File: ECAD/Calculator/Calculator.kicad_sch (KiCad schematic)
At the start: 30 parts, among them SW1 Switch_Tactile_ESwitch, SW10 Switch_Tactile_ESwitch, SW11 Switch_Tactile_ESwitch, SW12 Switch_Tactile_ESwitch, SW13 Switch_Tactile_ESwitch, SW14 Switch_Tactile_ESwitch, SW15 Switch_Tactile_ESwitch, SW16 Switch_Tactile_ESwitch, SW17 Switch_Tactile_ESwitch, SW18 Switch_Tactile_ESwitch, SW19 Switch_Tactile_ESwitch, SW2 Switch_Tactile_ESwitch, SW20 Switch_Tactile_ESwitch, SW3 Switch_Tactile_ESwitch, SW4 Switch_Tactile_ESwitch, SW5 Switch_Tactile_ESwitch, SW6 Switch_Tactile_ESwitch, SW7 Switch_Tactile_ESwitch, SW8 Switch_Tactile_ESwitch, SW9 Switch_Tactile_ESwitch

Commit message: Refactor Calculator schematic and library components
- Added multiple no-connect points in the Calculator schematic for better layout management.
- Updated the footprint properties for buttons to use "Button_Switch_Keyboard:SW_Cherry_MX_1.00u_PCB" instead of the previous "PCM_fab:Button_ESwitch_TL3315NF100Q_4.5x4.5mm".
- Introduced a new footprint for solder pads in the Calculator library.
- Created a new footprint library table for the Calculator project.
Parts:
- SW1, SW10, SW11, SW12, SW13, SW14, SW15, SW16, SW17, SW18, SW19, SW2, SW20, SW3, SW4, SW5, SW6, SW7, SW8, SW9: footprint PCM_fab:Button_ESwitch_TL3315NF100Q_4.5x4.5mm -> Button_Switch_Keyboard:SW_Cherry_MX_1.00u_PCB
- TP1, TP2, TP3, TP4, TP5, TP6, TP7, TP8, TP9: footprint (none) -> Calculator_lib:Solder_pad
- U1: footprint ESP32_30pin -> ESP32_Footprints:ESP32_30pin
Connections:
- no-connect marks 0 -> 12
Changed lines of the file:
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@@
 		(color 0 0 0 0)
 	)
+	(no_connect
+		(at 80.01 31.75)
+	)
+	(no_connect
+		(at 53.34 44.45)
+	)
+	(no_connect
+		(at 80.01 62.23)
+	)
+	(no_connect
+		(at 80.01 29.21)
+	)
+	(no_connect
+		(at 53.34 62.23)
+	)
+	(no_connect
+		(at 53.34 57.15)
+	)
+	(no_connect
+		(at 53.34 54.61)
+	)
+	(no_connect
+		(at 80.01 64.77)
+	)
+	(no_connect
+		(at 80.01 57.15)
+	)
+	(no_connect
+		(at 80.01 59.69)
+	)
+	(no_connect
+		(at 53.34 59.69)
+	)
+	(no_connect
+		(at 53.34 34.29)
+	)
 	(wire
 		(pts
@@
 			)
 		)
-		(property "Footprint" "PCM_fab:Button_ESwitch_TL3315NF100Q_4.5x4.5mm"
+		(property "Footprint" "Button_Switch_Keyboard:SW_Cherry_MX_1.00u_PCB"
 			(at 175.26 55.88 0)
 			(hide yes)
@@
 			)
 		)
-		(property "Footprint" "PCM_fab:Button_ESwitch_TL3315NF100Q_4.5x4.5mm"
+		(property "Footprint" "Button_Switch_Keyboard:SW_Cherry_MX_1.00u_PCB"
 			(at 129.54 78.74 0)
 			(hide yes)
@@
 			)
 		)
-		(property "Footprint" "PCM_fab:Button_ESwitch_TL3315NF100Q_4.5x4.5mm"
+		(property "Footprint" "Button_Switch_Keyboard:SW_Cherry_MX_1.00u_PCB"
 			(at 129.54 44.45 0)
 			(hide yes)
@@
 			)
 		)
-		(property "Footprint" ""
+		(property "Footprint" "Calculator_lib:Solder_pad"
 			(at 25.4 39.37 0)
 			(hide yes)
@@
 			)
 		)
-		(property "Footprint" ""
+		(property "Footprint" "Calculator_lib:Solder_pad"
 			(at 25.4 16.51 0)
 			(hide yes)
@@
 			)
 		)
-		(property "Footprint" ""
+		(property "Footprint" "Calculator_lib:Solder_pad"
 			(at 25.4 31.75 0)
 			(hide yes)
@@
 			)
 		)
-		(property "Footprint" ""
+		(property "Footprint" "Calculator_lib:Solder_pad"
 			(at 25.4 43.18 0)
 			(hide yes)
@@
 			)
 		)
-		(property "Footprint" "PCM_fab:Button_ESwitch_TL3315NF100Q_4.5x4.5mm"
+		(property "Footprint" "Button_Switch_Keyboard:SW_Cherry_MX_1.00u_PCB"
 			(at 129.54 67.31 0)
 			(hide yes)
@@
 			)
 		)
-		(property "Footprint" ""
+		(property "Footprint" "Calculator_lib:Solder_pad"
 			(at 25.4 12.7 0)
 			(hide yes)
@@
 			)
 		)
-		(property "Footprint" "PCM_fab:Button_ESwitch_TL3315NF100Q_4.5x4.5mm"
+		(property "Footprint" "Button_Switch_Keyboard:SW_Cherry_MX_1.00u_PCB"
 			(at 106.68 33.02 0)
 			(hide yes)
@@
 			)
 		)
-		(property "Footprint" "PCM_fab:Button_ESwitch_TL3315NF100Q_4.5x4.5mm"
+		(property "Footprint" "Button_Switch_Keyboard:SW_Cherry_MX_1.00u_PCB"
 			(at 106.68 55.88 0)
 			(hide yes)
@@
 			)
 		)
-		(property "Footprint" "PCM_fab:Button_ESwitch_TL3315NF100Q_4.5x4.5mm"
+		(property "Footprint" "Button_Switch_Keyboard:SW_Cherry_MX_1.00u_PCB"
 			(at 152.4 55.88 0)
 			(hide yes)
@@
 			)
 		)
-		(property "Footprint" "PCM_fab:Button_ESwitch_TL3315NF100Q_4.5x4.5mm"
+		(property "Footprint" "Button_Switch_Keyboard:SW_Cherry_MX_1.00u_PCB"
 			(at 129.54 55.88 0)
 			(hide yes)
@@
 			)
 		)
-		(property "Footprint" "PCM_fab:Button_ESwitch_TL3315NF100Q_4.5x4.5mm"
+		(property "Footprint" "Button_Switch_Keyboard:SW_Cherry_MX_1.00u_PCB"
 			(at 175.26 44.45 0)
 			(hide yes)
@@
 			)
 		)
-		(property "Footprint" "PCM_fab:Button_ESwitch_TL3315NF100Q_4.5x4.5mm"
+		(property "Footprint" "Button_Switch_Keyboard:SW_Cherry_MX_1.00u_PCB"
 			(at 152.4 44.45 0)
 			(hide yes)
@@
 			)
 		)
-		(property "Footprint" "PCM_fab:Button_ESwitch_TL3315NF100Q_4.5x4.5mm"
+		(property "Footprint" "Button_Switch_Keyboard:SW_Cherry_MX_1.00u_PCB"
 			(at 152.4 67.31 0)
 			(hide yes)
@@
 			)
 		)
-		(property "Footprint" "PCM_fab:Button_ESwitch_TL3315NF100Q_4.5x4.5mm"
+		(property "Footprint" "Button_Switch_Keyboard:SW_Cherry_MX_1.00u_PCB"
 			(at 175.26 67.31 0)
 			(hide yes)
@@
 			)
 		)
-		(property "Footprint" "ESP32_30pin"
+		(property "Footprint" "ESP32_Footprints:ESP32_30pin"
 			(at 66.675 19.05 90)
 			(show_name no)
@@
 			)
 		)
-		(property "Footprint" "PCM_fab:Button_ESwitch_TL3315NF100Q_4.5x4.5mm"
+		(property "Footprint" "Button_Switch_Keyboard:SW_Cherry_MX_1.00u_PCB"
 			(at 106.68 67.31 0)
 			(hide yes)
@@
 			)
 		)
-		(property "Footprint" ""
+		(property "Footprint" "Calculator_lib:Solder_pad"
 			(at 25.4 35.56 0)
 			(hide yes)
@@
 			)
 		)
-		(property "Footprint" ""
+		(property "Footprint" "Calculator_lib:Solder_pad"
 			(at 25.4 24.13 0)
 			(hide yes)
@@
 			)
 		)
-		(property "Footprint" "PCM_fab:Button_ESwitch_TL3315NF100Q_4.5x4.5mm"
+		(property "Footprint" "Button_Switch_Keyboard:SW_Cherry_MX_1.00u_PCB"
 			(at 106.68 78.74 0)
 			(hide yes)
@@
 			)
 		)
-		(property "Footprint" ""
+		(property "Footprint" "Calculator_lib:Solder_pad"
 			(at 25.4 27.94 0)
 			(hide yes)
@@
 			)
 		)
-		(property "Footprint" "PCM_fab:Button_ESwitch_TL3315NF100Q_4.5x4.5mm"
+		(property "Footprint" "Button_Switch_Keyboard:SW_Cherry_MX_1.00u_PCB"
 			(at 152.4 78.74 0)
 			(hide yes)
@@
 			)
 		)
-		(property "Footprint" "PCM_fab:Button_ESwitch_TL3315NF100Q_4.5x4.5mm"
+		(property "Footprint" "Button_Switch_Keyboard:SW_Cherry_MX_1.00u_PCB"
 			(at 129.54 33.02 0)
 			(hide yes)
@@
 			)
 		)
-		(property "Footprint" ""
+		(property "Footprint" "Calculator_lib:Solder_pad"
 			(at 25.4 20.32 0)
 			(hide yes)
@@
 			)
 		)
-		(property "Footprint" "PCM_fab:Button_ESwitch_TL3315NF100Q_4.5x4.5mm"
+		(property "Footprint" "Button_Switch_Keyboard:SW_Cherry_MX_1.00u_PCB"
 			(at 106.68 44.45 0)
 			(hide yes)
@@
 			)
 		)
-		(property "Footprint" "PCM_fab:Button_ESwitch_TL3315NF100Q_4.5x4.5mm"
+		(property "Footprint" "Button_Switch_Keyboard:SW_Cherry_MX_1.00u_PCB"
 			(at 152.4 33.02 0)
 			(hide yes)
@@
 			)
 		)
-		(property "Footprint" "PCM_fab:Button_ESwitch_TL3315NF100Q_4.5x4.5mm"
+		(property "Footprint" "Button_Switch_Keyboard:SW_Cherry_MX_1.00u_PCB"
 			(at 175.26 33.02 0)
 			(hide yes)
@@
 			)
 		)
-		(property "Footprint" "PCM_fab:Button_ESwitch_TL3315NF100Q_4.5x4.5mm"
+		(property "Footprint" "Button_Switch_Keyboard:SW_Cherry_MX_1.00u_PCB"
 			(at 175.26 78.74 0)
 			(hide yes)

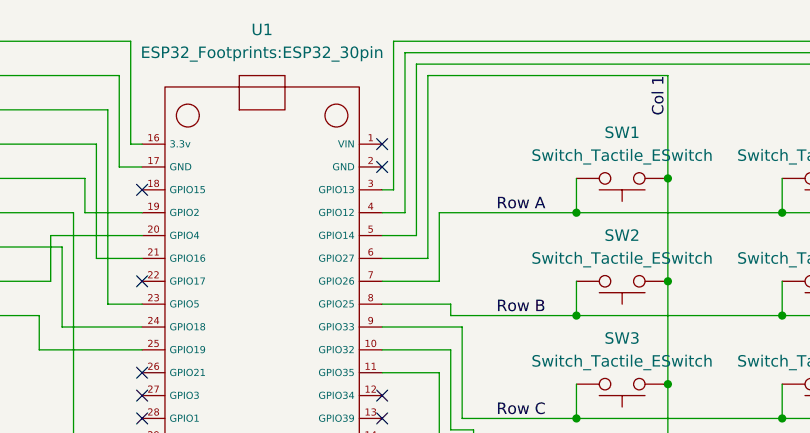
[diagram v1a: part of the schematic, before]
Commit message: Refactor schematic: Remove unnecessary wires and update connections in Calculator.kicad_sch Added keyboard matrix wiring in PCB and mounting holes for enclosure
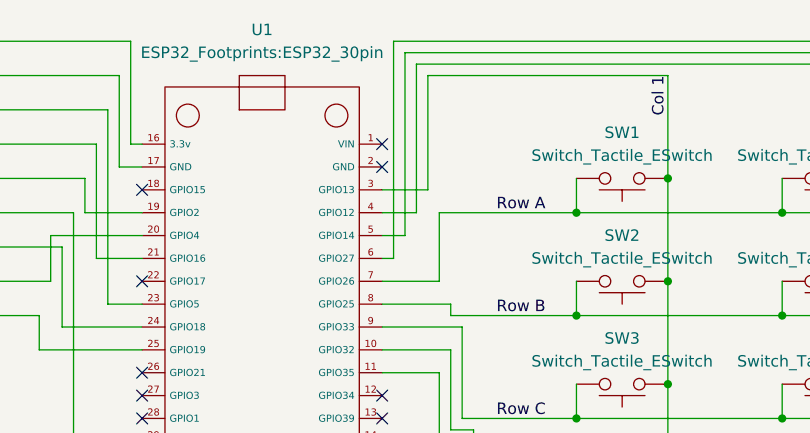
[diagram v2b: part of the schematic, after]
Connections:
- net Col 1: now also U1.3 (GPIO13); no longer U1.6 (GPIO27)
- net Col 2: now also U1.4 (GPIO12); no longer U1.5 (GPIO14)
- net Col 3: now also U1.5 (GPIO14); no longer U1.4 (GPIO12)
- net Col 4: now also U1.6 (GPIO27); no longer U1.3 (GPIO13)
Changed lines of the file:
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@@
-	(wire
-		(pts
-			(xy 80.01 36.83) (xy 82.55 36.83)
-		)
-		(stroke
-			(width 0)
-			(type default)
-		)
-	)
 	(wire
 		(pts
@@
 	(wire
 		(pts
-			(xy 83.82 39.37) (xy 80.01 39.37)
-		)
-		(stroke
-			(width 0)
-			(type default)
-		)
-	)
-	(wire
-		(pts
 			(xy 111.76 44.45) (xy 111.76 55.88)
 		)
@@
 	(wire
 		(pts
-			(xy 81.28 34.29) (xy 80.01 34.29)
-		)
-		(stroke
-			(width 0)
-			(type default)
-		)
-	)
-	(wire
-		(pts
 			(xy 147.32 36.83) (xy 170.18 36.83)
 		)
@@
 	(wire
 		(pts
+			(xy 83.82 36.83) (xy 80.01 36.83)
+		)
+		(stroke
+			(width 0)
+			(type default)
+		)
+	)
+	(wire
+		(pts
 			(xy 44.45 49.53) (xy 53.34 49.53)
 		)
@@
 	(wire
 		(pts
+			(xy 81.28 41.91) (xy 80.01 41.91)
+		)
+		(stroke
+			(width 0)
+			(type default)
+		)
+	)
+	(wire
+		(pts
 			(xy 25.4 21.59) (xy 50.8 21.59)
 		)
@@
 	(wire
 		(pts
-			(xy 85.09 21.59) (xy 85.09 41.91)
-		)
-		(stroke
-			(width 0)
-			(type default)
-		)
-	)
-	(wire
-		(pts
 			(xy 180.34 44.45) (xy 180.34 55.88)
 		)
@@
 	(wire
 		(pts
-			(xy 82.55 19.05) (xy 82.55 36.83)
-		)
-		(stroke
-			(width 0)
-			(type default)
-		)
-	)
-	(wire
-		(pts
 			(xy 134.62 55.88) (xy 134.62 67.31)
 		)
@@
 	(wire
 		(pts
-			(xy 81.28 17.78) (xy 81.28 34.29)
-		)
-		(stroke
-			(width 0)
-			(type default)
-		)
-	)
-	(wire
-		(pts
 			(xy 44.45 40.64) (xy 44.45 49.53)
 		)
@@
 	(wire
 		(pts
+			(xy 85.09 21.59) (xy 85.09 34.29)
+		)
+		(stroke
+			(width 0)
+			(type default)
+		)
+	)
+	(wire
+		(pts
 			(xy 80.01 54.61) (xy 86.36 54.61)
 		)
@@
 	(wire
 		(pts
-			(xy 85.09 41.91) (xy 80.01 41.91)
-		)
-		(stroke
-			(width 0)
-			(type default)
-		)
-	)
-	(wire
-		(pts
 			(xy 50.8 21.59) (xy 50.8 31.75)
 		)
@@
 	(wire
 		(pts
+			(xy 83.82 20.32) (xy 83.82 36.83)
+		)
+		(stroke
+			(width 0)
+			(type default)
+		)
+	)
+	(wire
+		(pts
 			(xy 134.62 67.31) (xy 134.62 78.74)
 		)
@@
 	(wire
 		(pts
+			(xy 82.55 19.05) (xy 82.55 39.37)
+		)
+		(stroke
+			(width 0)
+			(type default)
+		)
+	)
+	(wire
+		(pts
 			(xy 86.36 54.61) (xy 86.36 62.23)
 		)
@@
 	(wire
 		(pts
-			(xy 83.82 20.32) (xy 83.82 39.37)
-		)
-		(stroke
-			(width 0)
-			(type default)
-		)
-	)
-	(wire
-		(pts
 			(xy 180.34 67.31) (xy 180.34 78.74)
 		)
@@
 	(wire
 		(pts
+			(xy 82.55 39.37) (xy 80.01 39.37)
+		)
+		(stroke
+			(width 0)
+			(type default)
+		)
+	)
+	(wire
+		(pts
 			(xy 87.63 52.07) (xy 87.63 60.96)
 		)
@@
 	(wire
 		(pts
+			(xy 85.09 34.29) (xy 80.01 34.29)
+		)
+		(stroke
+			(width 0)
+			(type default)
+		)
+	)
+	(wire
+		(pts
 			(xy 180.34 33.02) (xy 180.34 44.45)
 		)
@@
 		)
 		(stroke
+			(width 0)
+			(type default)
+		)
+	)
+	(wire
+		(pts
+			(xy 81.28 17.78) (xy 81.28 41.91)
+		)
+		(stroke

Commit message: Changed Various GPIO pins to avoid issures with missing pull-up resistors, and flash pins
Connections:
- net Col 2: now also U1.29 (GPIO22); no longer U1.4 (GPIO12)
- net Row E: now also U1.26 (GPIO21); no longer U1.11 (GPIO35)
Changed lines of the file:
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@@
+	)
+	(no_connect
+		(at 80.01 54.61)
 	)
 	(no_connect
@@
 	)
 	(no_connect
-		(at 53.34 62.23)
+		(at 80.01 36.83)
 	)
 	(no_connect
@@
 	)
 	(no_connect
-		(at 53.34 54.61)
-	)
-	(no_connect
 		(at 80.01 64.77)
 	)
@@
 	(wire
 		(pts
+			(xy 50.8 73.66) (xy 83.82 73.66)
+		)
+		(stroke
+			(width 0)
+			(type default)
+		)
+	)
+	(wire
+		(pts
 			(xy 82.55 19.05) (xy 157.48 19.05)
 		)
@@
 	(wire
 		(pts
-			(xy 83.82 36.83) (xy 80.01 36.83)
+			(xy 50.8 73.66) (xy 50.8 62.23)
 		)
 		(stroke
@@
 	(wire
 		(pts
-			(xy 92.71 82.55) (xy 92.71 72.39)
-		)
-		(stroke
-			(width 0)
-			(type default)
-		)
-	)
-	(wire
-		(pts
-			(xy 88.9 72.39) (xy 92.71 72.39)
-		)
-		(stroke
-			(width 0)
-			(type default)
-		)
-	)
-	(wire
-		(pts
 			(xy 134.62 55.88) (xy 134.62 67.31)
 		)
@@
 	(wire
 		(pts
-			(xy 86.36 62.23) (xy 88.9 62.23)
-		)
-		(stroke
-			(width 0)
-			(type default)
-		)
-	)
-	(wire
-		(pts
 			(xy 44.45 40.64) (xy 44.45 49.53)
 		)
@@
 	(wire
 		(pts
-			(xy 80.01 54.61) (xy 86.36 54.61)
-		)
-		(stroke
-			(width 0)
-			(type default)
-		)
-	)
-	(wire
-		(pts
 			(xy 134.62 44.45) (xy 134.62 55.88)
 		)
@@
 	(wire
 		(pts
+			(xy 50.8 62.23) (xy 53.34 62.23)
+		)
+		(stroke
+			(width 0)
+			(type default)
+		)
+	)
+	(wire
+		(pts
 			(xy 147.32 71.12) (xy 170.18 71.12)
 		)
@@
 	(wire
 		(pts
-			(xy 83.82 20.32) (xy 83.82 36.83)
+			(xy 83.82 20.32) (xy 83.82 73.66)
 		)
 		(stroke
@@
 	(wire
 		(pts
+			(xy 49.53 54.61) (xy 49.53 82.55)
+		)
+		(stroke
+			(width 0)
+			(type default)
+		)
+	)
+	(wire
+		(pts
 			(xy 147.32 36.83) (xy 147.32 33.02)
 		)
@@
 	(wire
 		(pts
-			(xy 86.36 54.61) (xy 86.36 62.23)
-		)
-		(stroke
-			(width 0)
-			(type default)
-		)
-	)
-	(wire
-		(pts
 			(xy 170.18 48.26) (xy 170.18 44.45)
 		)
@@
 	(wire
 		(pts
-			(xy 88.9 62.23) (xy 88.9 72.39)
-		)
-		(stroke
-			(width 0)
-			(type default)
-		)
-	)
-	(wire
-		(pts
 			(xy 157.48 33.02) (xy 157.48 44.45)
 		)
@@
 	(wire
 		(pts
+			(xy 53.34 54.61) (xy 49.53 54.61)
+		)
+		(stroke
+			(width 0)
+			(type default)
+		)
+	)
+	(wire
+		(pts
 			(xy 180.34 17.78) (xy 180.34 33.02)
 		)
@@
 	(wire
 		(pts
-			(xy 92.71 82.55) (xy 101.6 82.55)
-		)
-		(stroke
+			(xy 49.53 82.55) (xy 101.6 82.55)
+		)
+		(stroke

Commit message: Update ESP32_30pin footprint and add new MX-Solderable-1U footprint
- Updated ESP32_30pin.kicad_mod with new version, generator version, and 3D model
- Added new MX-Solderable-1U.kicad_mod footprint with detailed properties and pads.
- Introduced new 3D models for ESP32-30pin and Cherry MX switches.
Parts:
- SW1, SW10, SW11, SW12, SW13, SW14, SW15, SW16, SW17, SW18, SW19, SW2, SW20, SW3, SW4, SW5, SW6, SW7, SW8, SW9: footprint Button_Switch_Keyboard:SW_Cherry_MX_1.00u_PCB -> Calculator_lib:MX-Solderable-1U
- U1: footprint ESP32_Footprints:ESP32_30pin -> Calculator_lib:ESP32_30pin
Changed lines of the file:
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@@
 			)
 		)
-		(property "Footprint" "Button_Switch_Keyboard:SW_Cherry_MX_1.00u_PCB"
+		(property "Footprint" "Calculator_lib:MX-Solderable-1U"
 			(at 175.26 55.88 0)
 			(hide yes)
@@
 			)
 		)
-		(property "Footprint" "Button_Switch_Keyboard:SW_Cherry_MX_1.00u_PCB"
+		(property "Footprint" "Calculator_lib:MX-Solderable-1U"
 			(at 129.54 78.74 0)
 			(hide yes)
@@
 			)
 		)
-		(property "Footprint" "Button_Switch_Keyboard:SW_Cherry_MX_1.00u_PCB"
+		(property "Footprint" "Calculator_lib:MX-Solderable-1U"
 			(at 129.54 44.45 0)
 			(hide yes)
@@
 			)
 		)
-		(property "Footprint" "Button_Switch_Keyboard:SW_Cherry_MX_1.00u_PCB"
+		(property "Footprint" "Calculator_lib:MX-Solderable-1U"
 			(at 129.54 67.31 0)
 			(hide yes)
@@
 			)
 		)
-		(property "Footprint" "Button_Switch_Keyboard:SW_Cherry_MX_1.00u_PCB"
+		(property "Footprint" "Calculator_lib:MX-Solderable-1U"
 			(at 106.68 33.02 0)
 			(hide yes)
@@
 			)
 		)
-		(property "Footprint" "Button_Switch_Keyboard:SW_Cherry_MX_1.00u_PCB"
+		(property "Footprint" "Calculator_lib:MX-Solderable-1U"
 			(at 106.68 55.88 0)
 			(hide yes)
@@
 			)
 		)
-		(property "Footprint" "Button_Switch_Keyboard:SW_Cherry_MX_1.00u_PCB"
+		(property "Footprint" "Calculator_lib:MX-Solderable-1U"
 			(at 152.4 55.88 0)
 			(hide yes)
@@
 			)
 		)
-		(property "Footprint" "Button_Switch_Keyboard:SW_Cherry_MX_1.00u_PCB"
+		(property "Footprint" "Calculator_lib:MX-Solderable-1U"
 			(at 129.54 55.88 0)
 			(hide yes)
@@
 			)
 		)
-		(property "Footprint" "Button_Switch_Keyboard:SW_Cherry_MX_1.00u_PCB"
+		(property "Footprint" "Calculator_lib:MX-Solderable-1U"
 			(at 175.26 44.45 0)
 			(hide yes)
@@
 			)
 		)
-		(property "Footprint" "Button_Switch_Keyboard:SW_Cherry_MX_1.00u_PCB"
+		(property "Footprint" "Calculator_lib:MX-Solderable-1U"
 			(at 152.4 44.45 0)
 			(hide yes)
@@
 			)
 		)
-		(property "Footprint" "Button_Switch_Keyboard:SW_Cherry_MX_1.00u_PCB"
+		(property "Footprint" "Calculator_lib:MX-Solderable-1U"
 			(at 152.4 67.31 0)
 			(hide yes)
@@
 			)
 		)
-		(property "Footprint" "Button_Switch_Keyboard:SW_Cherry_MX_1.00u_PCB"
+		(property "Footprint" "Calculator_lib:MX-Solderable-1U"
 			(at 175.26 67.31 0)
 			(hide yes)
@@
 			)
 		)
-		(property "Footprint" "ESP32_Footprints:ESP32_30pin"
+		(property "Footprint" "Calculator_lib:ESP32_30pin"
 			(at 66.675 19.05 90)
 			(show_name no)
@@
 			)
 		)
-		(property "Footprint" "Button_Switch_Keyboard:SW_Cherry_MX_1.00u_PCB"
+		(property "Footprint" "Calculator_lib:MX-Solderable-1U"
 			(at 106.68 67.31 0)
 			(hide yes)
@@
 			)
 		)
-		(property "Footprint" "Button_Switch_Keyboard:SW_Cherry_MX_1.00u_PCB"
+		(property "Footprint" "Calculator_lib:MX-Solderable-1U"
 			(at 106.68 78.74 0)
 			(hide yes)
@@
 			)
 		)
-		(property "Footprint" "Button_Switch_Keyboard:SW_Cherry_MX_1.00u_PCB"
+		(property "Footprint" "Calculator_lib:MX-Solderable-1U"
 			(at 152.4 78.74 0)
 			(hide yes)
@@
 			)
 		)
-		(property "Footprint" "Button_Switch_Keyboard:SW_Cherry_MX_1.00u_PCB"
+		(property "Footprint" "Calculator_lib:MX-Solderable-1U"
 			(at 129.54 33.02 0)
 			(hide yes)
@@
 			)
 		)
-		(property "Footprint" "Button_Switch_Keyboard:SW_Cherry_MX_1.00u_PCB"
+		(property "Footprint" "Calculator_lib:MX-Solderable-1U"
 			(at 106.68 44.45 0)
 			(hide yes)
@@
 			)
 		)
-		(property "Footprint" "Button_Switch_Keyboard:SW_Cherry_MX_1.00u_PCB"
+		(property "Footprint" "Calculator_lib:MX-Solderable-1U"
 			(at 152.4 33.02 0)
 			(hide yes)
@@
 			)
 		)
-		(property "Footprint" "Button_Switch_Keyboard:SW_Cherry_MX_1.00u_PCB"
+		(property "Footprint" "Calculator_lib:MX-Solderable-1U"
 			(at 175.26 33.02 0)
 			(hide yes)
@@
 			)
 		)
-		(property "Footprint" "Button_Switch_Keyboard:SW_Cherry_MX_1.00u_PCB"
+		(property "Footprint" "Calculator_lib:MX-Solderable-1U"
 			(at 175.26 78.74 0)
 			(hide yes)
